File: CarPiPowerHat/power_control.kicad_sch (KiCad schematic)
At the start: 20 parts, among them U3 LM3480-5.0, U4 ATtiny45V-10X

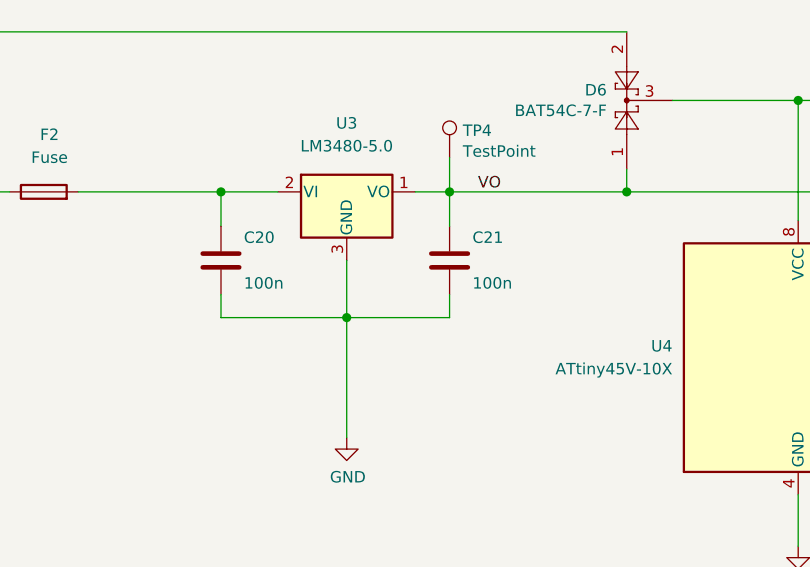
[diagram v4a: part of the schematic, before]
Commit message: Added part numbers
* Selected parts from lcsc
* Checked footprints
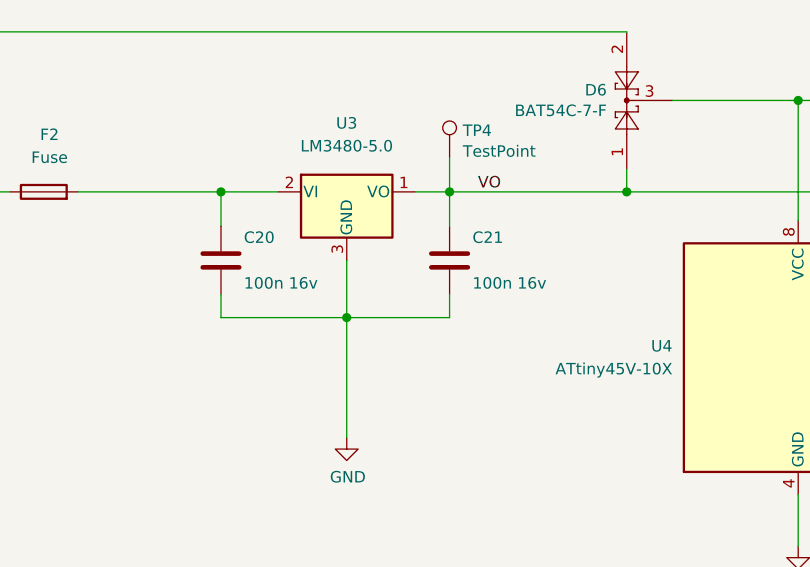
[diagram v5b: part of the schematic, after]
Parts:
- C20, C21: value 100n -> 100n 16v
- R11: LCSC (none) -> C270649
- U4: LCSC (none) -> C144181
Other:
- title: (none) -> Power Control Circuit
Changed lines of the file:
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@@
 (kicad_sch (version 20210621) (generator eeschema)
   (paper "A4")
+  (title_block
+    (title "Power Control Circuit")
+    (date "2021-08-24")
+    (rev "1")
+  )
   (junction (at 55.245 43.815) (diameter 1.016) (color 0 0 0 0))
   (junction (at 69.215 57.785) (diameter 1.016) (color 0 0 0 0))
@@
       (effects (font (size 1.27 1.27)) hide)
     )
-    (property "LCSC" "" (id 4) (at 181.61 47.625 0)
+    (property "LCSC" "C270649" (id 4) (at 181.61 47.625 0)
       (effects (font (size 1.27 1.27)) hide)
     )
@@
       (effects (font (size 1.27 1.27)) (justify left))
     )
-    (property "Value" "100n" (id 1) (at 57.785 53.975 0)
+    (property "Value" "100n 16v" (id 1) (at 57.785 53.975 0)
       (effects (font (size 1.27 1.27)) (justify left))
     )
@@
       (effects (font (size 1.27 1.27)) (justify left))
     )
-    (property "Value" "100n" (id 1) (at 83.185 53.975 0)
+    (property "Value" "100n 16v" (id 1) (at 83.185 53.975 0)
       (effects (font (size 1.27 1.27)) (justify left))
     )
@@
       (effects (font (size 1.27 1.27)) hide)
     )
+    (property "LCSC" "C144181" (id 4) (at 119.38 62.23 0)
+      (effects (font (size 1.27 1.27)) hide)
+    )

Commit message: Fixed some bugs, not done yet
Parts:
- added J11: Conn_01x06_Male, Connector_PinHeader_2.54mm:PinHeader_2x03_P2.54mm_Vertical, symbol Connector:Conn_01x06_Male
- D6: LCSC C37704 -> C181200
- F1: renamed from F2; footprint Fuse:Fuse_Littelfuse-NANO2-451_453 -> Fuse:Fuse_1206_3216Metric_Pad1.42x1.75mm_HandSolder; LCSC (none) -> C206984
- U2: renamed from U4; value ATtiny45V-10X -> ATtiny45V-20SU; footprint Package_SO:TSSOP-8_4.4x3mm_P0.65mm -> Package_SO:SOIC-8W_5.3x5.3mm_P1.27mm; LCSC C144181 -> C62689
- renumbered C20 to C31, C21 to C32, D1 to D10, D2 to D9, R16 to R19, R13 to R21, R11 to R23, R18 to R24, R14 to R3, R17 to R4, R28 to R5, R19 to R6, R15 to R7, TP4 to TP5, U3 to U7
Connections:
- net GND: now also J11.6 (Pin_6)
- net VCC: now also J11.2 (Pin_2)
- net SCK: now reaches R5.1, R6.1, U2.7 (PB2)
- net SCK: now also J11.3 (Pin_3)
- net MOSI: now reaches R3.1, U2.5 (AREF/PB0)
- net MOSI: now also J11.4 (Pin_4)
- net RESET: now reaches R4.2, U2.1 (~{RESET}/PB5)
- net RESET: now also J11.5 (Pin_5)
- net MISO: now reaches R24.1, U2.6 (PB1)
- net MISO: now also J11.1 (Pin_1)
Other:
- moved on the sheet: D10, D9, R19, R21, R23, R24, R3, R4, R5, R6, R7, TP6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

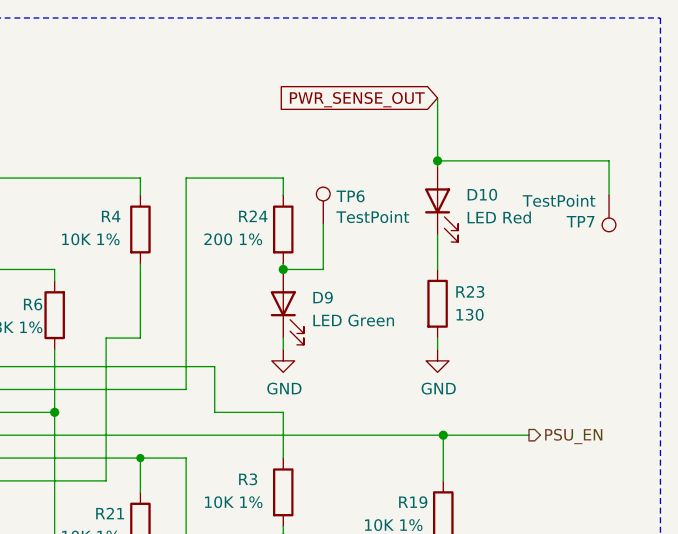
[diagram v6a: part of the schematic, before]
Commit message: Some rerouting
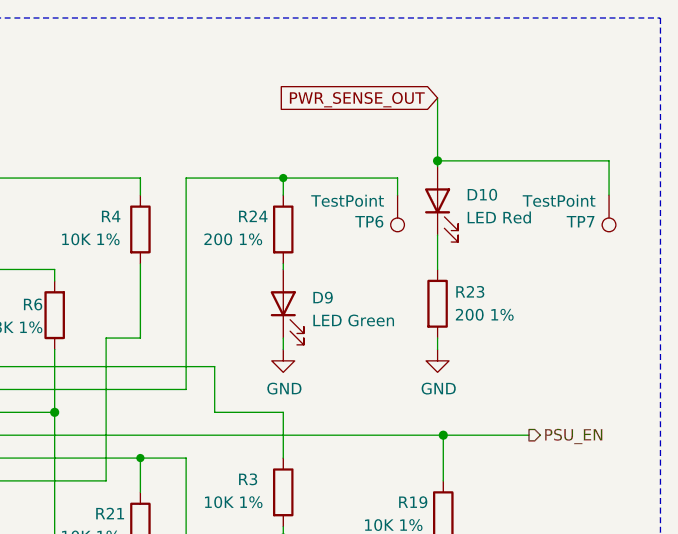
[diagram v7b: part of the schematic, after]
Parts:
- R23: value 130 -> 200 1%; LCSC C270649 -> 9239367
- TP5, TP6, TP7: footprint TestPoint:TestPoint_Pad_2.0x2.0mm -> TestPoint:TestPoint_Pad_D1.0mm
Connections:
- net MISO: now also TP6.1
- net at D9.2 (A), R24.2: no longer TP6.1
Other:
- moved on the sheet: TP6
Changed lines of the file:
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@@
   (junction (at 149.225 59.69) (diameter 1.016) (color 0 0 0 0))
   (junction (at 158.75 64.77) (diameter 0.9144) (color 0 0 0 0))
-  (junction (at 174.625 43.815) (diameter 1.016) (color 0 0 0 0))
+  (junction (at 174.625 33.655) (diameter 0.9144) (color 0 0 0 0))
   (junction (at 174.625 73.66) (diameter 1.016) (color 0 0 0 0))
   (junction (at 191.77 31.75) (diameter 1.016) (color 0 0 0 0))
@@
     (stroke (width 0) (type solid) (color 0 0 0 0))
   )
+  (wire (pts (xy 174.625 33.655) (xy 187.325 33.655))
+    (stroke (width 0) (type solid) (color 0 0 0 0))
+  )
   (wire (pts (xy 174.625 43.815) (xy 174.625 43.18))
     (stroke (width 0) (type solid) (color 0 0 0 0))
@@
     (stroke (width 0) (type solid) (color 0 0 0 0))
   )
-  (wire (pts (xy 179.07 38.735) (xy 179.07 43.815))
-    (stroke (width 0) (type solid) (color 0 0 0 0))
-  )
-  (wire (pts (xy 179.07 43.815) (xy 174.625 43.815))
-    (stroke (width 0) (type solid) (color 0 0 0 0))
-  )
   (wire (pts (xy 180.34 73.66) (xy 174.625 73.66))
     (stroke (width 0) (type solid) (color 0 0 0 0))
@@
   )
   (wire (pts (xy 180.34 94.615) (xy 198.12 94.615))
+    (stroke (width 0) (type solid) (color 0 0 0 0))
+  )
+  (wire (pts (xy 187.325 33.655) (xy 187.325 35.56))
     (stroke (width 0) (type solid) (color 0 0 0 0))
   )
@@
       (effects (font (size 1.27 1.27)) (justify left))
     )
-    (property "Footprint" "TestPoint:TestPoint_Pad_2.0x2.0mm" (id 2) (at 85.725 40.005 0)
+    (property "Footprint" "TestPoint:TestPoint_Pad_D1.0mm" (id 2) (at 85.725 40.005 0)
       (effects (font (size 1.27 1.27)) hide)
     )
@@
     (pin "1")
   )
-  (symbol (lib_id "Connector:TestPoint") (at 179.07 38.735 0) (unit 1)
-    (in_bom yes) (on_board yes)
-    (property "Reference" "TP6" (id 0) (at 180.5432 35.7378 0)
-      (effects (font (size 1.27 1.27)) (justify left))
-    )
-    (property "Value" "TestPoint" (id 1) (at 180.5432 38.0492 0)
-      (effects (font (size 1.27 1.27)) (justify left))
-    )
-    (property "Footprint" "TestPoint:TestPoint_Pad_2.0x2.0mm" (id 2) (at 184.15 38.735 0)
-      (effects (font (size 1.27 1.27)) hide)
-    )
-    (property "Datasheet" "~" (id 3) (at 184.15 38.735 0)
-      (effects (font (size 1.27 1.27)) hide)
-    )
-    (property "Field4" "nf" (id 4) (at 179.07 38.735 0)
-      (effects (font (size 1.27 1.27)) hide)
-    )
-    (property "Field5" "nf" (id 5) (at 179.07 38.735 0)
-      (effects (font (size 1.27 1.27)) hide)
-    )
-    (property "Field6" "nf" (id 6) (at 179.07 38.735 0)
-      (effects (font (size 1.27 1.27)) hide)
-    )
-    (property "Field7" "nf" (id 7) (at 179.07 38.735 0)
+  (symbol (lib_id "Connector:TestPoint") (at 187.325 35.56 180) (unit 1)
+    (in_bom yes) (on_board yes)
+    (property "Reference" "TP6" (id 0) (at 185.8518 38.5572 0)
+      (effects (font (size 1.27 1.27)) (justify left))
+    )
+    (property "Value" "TestPoint" (id 1) (at 185.8518 36.2458 0)
+      (effects (font (size 1.27 1.27)) (justify left))
+    )
+    (property "Footprint" "TestPoint:TestPoint_Pad_D1.0mm" (id 2) (at 182.245 35.56 0)
+      (effects (font (size 1.27 1.27)) hide)
+    )
+    (property "Datasheet" "~" (id 3) (at 182.245 35.56 0)
+      (effects (font (size 1.27 1.27)) hide)
+    )
+    (property "Field4" "nf" (id 4) (at 187.325 35.56 0)
+      (effects (font (size 1.27 1.27)) hide)
+    )
+    (property "Field5" "nf" (id 5) (at 187.325 35.56 0)
+      (effects (font (size 1.27 1.27)) hide)
+    )
+    (property "Field6" "nf" (id 6) (at 187.325 35.56 0)
+      (effects (font (size 1.27 1.27)) hide)
+    )
+    (property "Field7" "nf" (id 7) (at 187.325 35.56 0)
       (effects (font (size 1.27 1.27)) hide)
     )
@@
       (effects (font (size 1.27 1.27)) (justify left))
     )
-    (property "Footprint" "TestPoint:TestPoint_Pad_2.0x2.0mm" (id 2) (at 205.74 35.56 0)
+    (property "Footprint" "TestPoint:TestPoint_Pad_D1.0mm" (id 2) (at 205.74 35.56 0)
       (effects (font (size 1.27 1.27)) hide)
     )
@@
       (effects (font (size 1.27 1.27)) (justify left))
     )
-    (property "Value" "130" (id 1) (at 193.675 48.895 0)
+    (property "Value" "200 1%" (id 1) (at 193.675 48.895 0)
       (effects (font (size 1.27 1.27)) (justify left))
     )
@@
       (effects (font (size 1.27 1.27)) hide)
     )
-    (property "LCSC" "C270649" (id 4) (at 191.77 47.625 0)
-      (effects (font (size 1.27 1.27)) hide)
-    )
+    (property "LCSC" "9239367" (id 4) (at 191.77 47.625 0)
+      (effects (font (size 1.27 1.27)) hide)
+    )

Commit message: Finalized 2.2
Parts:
- R23: LCSC 9239367 -> C25087
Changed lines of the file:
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@@
       (effects (font (size 1.27 1.27)) hide)
     )
-    (property "LCSC" "9239367" (id 4) (at 191.77 47.625 0)
+    (property "LCSC" "C25087" (id 4) (at 191.77 47.625 0)
       (effects (font (size 1.27 1.27)) hide)
     )
